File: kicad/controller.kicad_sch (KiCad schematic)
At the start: 33 parts, among them M5 Motor_DC, M6 Motor_DC, M7 Motor_DC, M8 Motor_DC, U10 DRV8833PW, U6 ESP32-DEVKITC, U8 GY-521

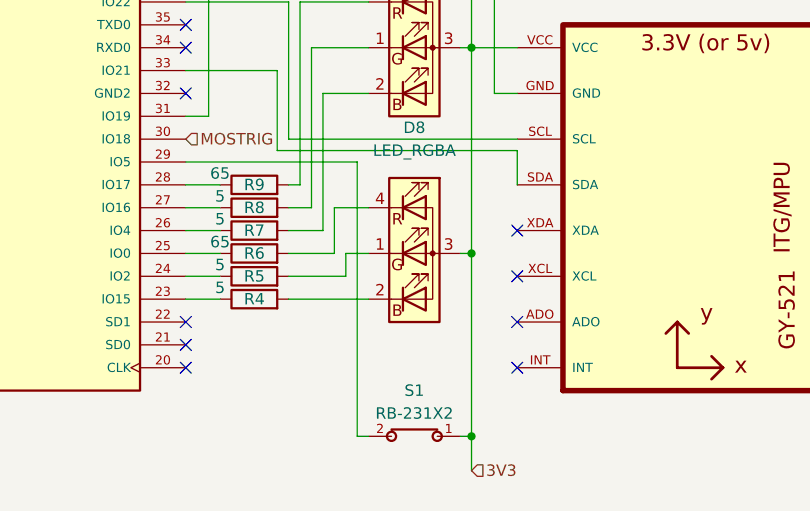
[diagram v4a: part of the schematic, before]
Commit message: Add tilt switch
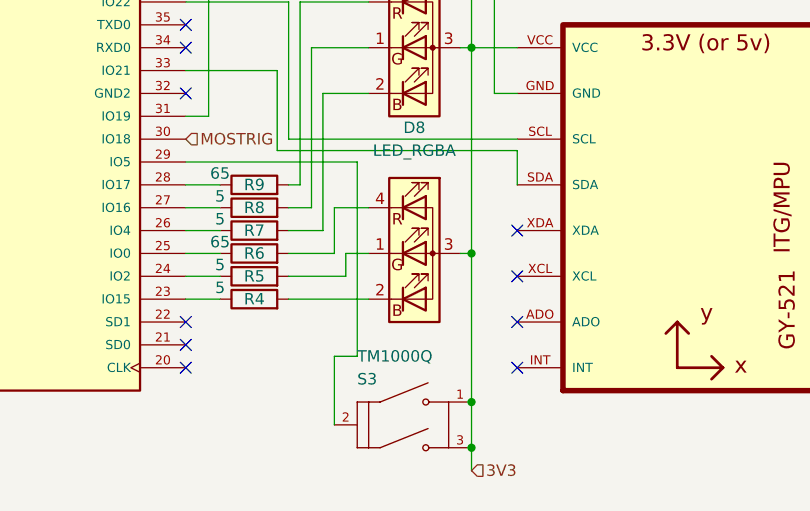
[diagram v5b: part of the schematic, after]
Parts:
- removed S1: RB-231X2, RB-231X2:SW_RB-231X2, symbol RB-231X2:RB-231X2
- added S3: TM1000Q, TM1000Q:SW_TM1000Q, symbol TM1000Q:TM1000Q
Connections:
- net 3V3: now also S3.1, S3.3
- net at U6.29 (IO5): now also S3.2
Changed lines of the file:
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@@
   (junction (at 115.57 74.93) (diameter 0) (color 0 0 0 0)
   )
+  (junction (at 213.36 139.7) (diameter 0) (color 0 0 0 0)
+  )
   (junction (at 125.73 87.63) (diameter 0) (color 0 0 0 0)
   )
@@
   (junction (at 124.46 107.95) (diameter 0) (color 0 0 0 0)
   )
+  (junction (at 213.36 134.62) (diameter 0) (color 0 0 0 0)
+  )
   (junction (at 125.73 127) (diameter 0) (color 0 0 0 0)
   )
@@
   )
   (junction (at 181.61 85.09) (diameter 0) (color 0 0 0 0)
-  )
-  (junction (at 213.36 138.43) (diameter 0) (color 0 0 0 0)
   )
   (junction (at 213.36 95.25) (diameter 0) (color 0 0 0 0)
@@
     (stroke (width 0) (type default))
   )
+  (wire (pts (xy 213.36 139.7) (xy 213.36 142.24))
+    (stroke (width 0) (type default))
+  )
   (wire (pts (xy 77.47 63.5) (xy 77.47 127))
     (stroke (width 0) (type default))
@@
     (stroke (width 0) (type default))
   )
-  (wire (pts (xy 212.09 138.43) (xy 213.36 138.43))
-    (stroke (width 0) (type default))
-  )
   (wire (pts (xy 80.01 74.93) (xy 76.2 74.93))
     (stroke (width 0) (type default))
@@
     (stroke (width 0) (type default))
   )
-  (wire (pts (xy 213.36 118.11) (xy 213.36 138.43))
+  (wire (pts (xy 213.36 118.11) (xy 213.36 134.62))
     (stroke (width 0) (type default))
   )
@@
     (stroke (width 0) (type default))
   )
+  (wire (pts (xy 213.36 134.62) (xy 213.36 139.7))
+    (stroke (width 0) (type default))
+  )
   (wire (pts (xy 121.92 92.71) (xy 121.92 96.52))
     (stroke (width 0) (type default))
@@
     (stroke (width 0) (type default))
   )
-  (wire (pts (xy 213.36 138.43) (xy 213.36 142.24))
-    (stroke (width 0) (type default))
-  )
   (wire (pts (xy 194.31 110.49) (xy 194.31 90.17))
     (stroke (width 0) (type default))
@@
     (stroke (width 0) (type default))
   )
-  (wire (pts (xy 200.66 107.95) (xy 200.66 138.43))
+  (wire (pts (xy 200.66 107.95) (xy 200.66 129.54))
     (stroke (width 0) (type default))
   )
@@
     (stroke (width 0) (type default))
   )
-  (wire (pts (xy 200.66 138.43) (xy 201.93 138.43))
+  (wire (pts (xy 198.12 129.54) (xy 198.12 137.16))
     (stroke (width 0) (type default))
   )
@@
   )
   (wire (pts (xy 57.15 77.47) (xy 80.01 77.47))
+    (stroke (width 0) (type default))
+  )
+  (wire (pts (xy 200.66 129.54) (xy 198.12 129.54))
     (stroke (width 0) (type default))
   )
@@
     )
   )
+  (symbol (lib_id "TM1000Q:TM1000Q") (at 205.74 137.16 0) (unit 1)
+    (in_bom yes) (on_board yes) (dnp no)
+    (property "Reference" "S3" (at 200.66 132.08 0)
+      (effects (font (size 1.27 1.27)) (justify left))
+    )
+    (property "Value" "TM1000Q" (at 200.66 129.54 0)
+      (effects (font (size 1.27 1.27)) (justify left))
+    )
+    (property "Footprint" "TM1000Q:SW_TM1000Q" (at 205.74 137.16 0)
+      (effects (font (size 1.27 1.27)) (justify bottom) hide)
+    )
+    (property "Datasheet" "" (at 205.74 137.16 0)
+      (effects (font (size 1.27 1.27)) hide)
+    )
+    (property "MF" "E-Switch" (at 205.74 137.16 0)
+      (effects (font (size 1.27 1.27)) (justify bottom) hide)
+    )
+    (property "MAXIMUM_PACKAGE_HEIGHT" "6.5mm" (at 205.74 137.16 0)
+      (effects (font (size 1.27 1.27)) (justify bottom) hide)
+    )
+    (property "Package" "SIP-3 E-Switch" (at 205.74 137.16 0)
+      (effects (font (size 1.27 1.27)) (justify bottom) hide)
+    )
+    (property "Price" "None" (at 205.74 137.16 0)
+      (effects (font (size 1.27 1.27)) (justify bottom) hide)
+    )
+    (property "Check_prices" "https://www.snapeda.com/parts/TM1000Q/E-Switch/view-part/?ref=eda" (at 205.74 137.16 0)
+      (effects (font (size 1.27 1.27)) (justify bottom) hide)
+    )
+    (property "STANDARD" "Manufacturer Recommendations" (at 205.74 137.16 0)
+      (effects (font (size 1.27 1.27)) (justify bottom) hide)
+    )
+    (property "PARTREV" "-" (at 205.74 137.16 0)
+      (effects (font (size 1.27 1.27)) (justify bottom) hide)
+    )
+    (property "SnapEDA_Link" "https://www.snapeda.com/parts/TM1000Q/E-Switch/view-part/?ref=snap" (at 205.74 137.16 0)
+      (effects (font (size 1.27 1.27)) (justify bottom) hide)
+    )
+    (property "MP" "TM1000Q" (at 205.74 137.16 0)
+      (effects (font (size 1.27 1.27)) (justify bottom) hide)
+    )
+    (property "Purchase-URL" "https://www.snapeda.com/api/url_track_click_mouser/?unipart_id=649122&manufacturer=E-Switch&part_name=TM1000Q&search_term=tm1000q" (at 205.74 137.16 0)
+      (effects (font (size 1.27 1.27)) (justify bottom) hide)
+    )
+    (property "Description" "\nSWITCH TILT SPST\n" (at 205.74 137.16 0)
+      (effects (font (size 1.27 1.27)) (justify bottom) hide)
+    )
+    (property "MANUFACTURER" "E-Switch" (at 205.74 137.16 0)
+      (effects (font (size 1.27 1.27)) (justify bottom) hide)
+    )
+    (property "Availability" "In Stock" (at 205.74 137.16 0)
+      (effects (font (size 1.27 1.27)) (justify bottom) hide)
+    )
+    (property "SNAPEDA_PN" "TM1000Q" (at 205.74 137.16 0)
+      (effects (font (size 1.27 1.27)) (justify bottom) hide)
+    )
+    (pin "1")
+    (pin "2")
+    (pin "3")
+    (instances
+      (project "robot"
+        (path "/9f6eb88e-d254-4b8d-b64f-838940a89234/50902c9c-c184-4e8b-b7c8-1add935d161c"
+          (reference "S3") (unit 1)
+        )
+        (path "/9f6eb88e-d254-4b8d-b64f-838940a89234/50902c9c-c184-4e8b-b7c8-1add935d161c/8bca0bb0-49b9-4104-9510-11a298d1fb37"
+          (reference "S1") (unit 1)
+        )
+      )
+    )
+  )
   (symbol (lib_id "Motor:Motor_DC") (at 57.15 85.09 0) (unit 1)
     (in_bom yes) (on_board yes) (dnp no) (fields_autoplaced)
@@
         )
       )
-    )
-  )
-  (symbol (lib_id "RB-231X2:RB-231X2") (at 207.01 138.43 0) (unit 1)
-    (in_bom yes) (on_board yes) (dnp no) (fields_autoplaced)
-    (property "Reference" "S1" (at 207.01 133.35 0)
-      (effects (font (size 1.27 1.27)))
-    )
-    (property "Value" "RB-231X2" (at 207.01 135.89 0)
-      (effects (font (size 1.27 1.27)))
-    )
-    (property "Footprint" "RB-231X2:SW_RB-231X2" (at 207.01 138.43 0)
-      (effects (font (size 1.27 1.27)) (justify bottom) hide)
-    )
-    (property "Datasheet" "" (at 207.01 138.43 0)
-      (effects (font (size 1.27 1.27)) hide)
-    )
-    (property "MF" "C&K" (at 207.01 138.43 0)
-      (effects (font (size 1.27 1.27)) (justify bottom) hide)
-    )
-    (property "Description" "\nRolling Ball Tilt Switches\n" (at 207.01 138.43 0)
-      (effects (font (size 1.27 1.27)) (justify bottom) hide)
-    )
-    (property "Package" "Radial Side View  C&amp;K Components" (at 207.01 138.43 0)
-      (effects (font (size 1.27 1.27)) (justify bottom) hide)
-    )
-    (property "Price" "None" (at 207.01 138.43 0)
-      (effects (font (size 1.27 1.27)) (justify bottom) hide)
-    )
-    (property "Check_prices" "https://www.snapeda.com/parts/RB-231X2/C%2526K/view-part/?ref=eda" (at 207.01 138.43 0)
-      (effects (font (size 1.27 1.27)) (justify bottom) hide)
-    )
-    (property "SnapEDA_Link" "https://www.snapeda.com/parts/RB-231X2/C%2526K/view-part/?ref=snap" (at 207.01 138.43 0)
-      (effects (font (size 1.27 1.27)) (justify bottom) hide)
-    )
-    (property "MP" "RB-231X2" (at 207.01 138.43 0)
-      (effects (font (size 1.27 1.27)) (justify bottom) hide)
-    )
-    (property "Purchase-URL" "https://www.snapeda.com/api/url_track_click_mouser/?unipart_id=494671&manufacturer=C&amp;K&part_name=RB-231X2&search_term=rb231" (at 207.01 138.43 0)
-      (effects (font (size 1.27 1.27)) (justify bottom) hide)
-    )
-    (property "Availability" "In Stock" (at 207.01 138.43 0)
-      (effects (font (size 1.27 1.27)) (justify bottom) hide)
-    )
-    (property "MANUFACTURER" "CnK" (at 207.01 138.43 0)
-      (effects (font (size 1.27 1.27)) (justify bottom) hide)
-    )
-    (pin "1")
-    (pin "2")
-    (instances
-      (project "robot"
-        (path "/9f6eb88e-d254-4b8d-b64f-838940a89234/50902c9c-c184-4e8b-b7c8-1add935d161c"
-          (reference "S1") (unit 1)
-        )
-        (path "/9f6eb88e-d254-4b8d-b64f-838940a89234/50902c9c-c184-4e8b-b7c8-1add935d161c/8bca0bb0-49b9-4104-9510-11a298d1fb37"
-          (reference "S2") (unit 1)
-        )
-      )

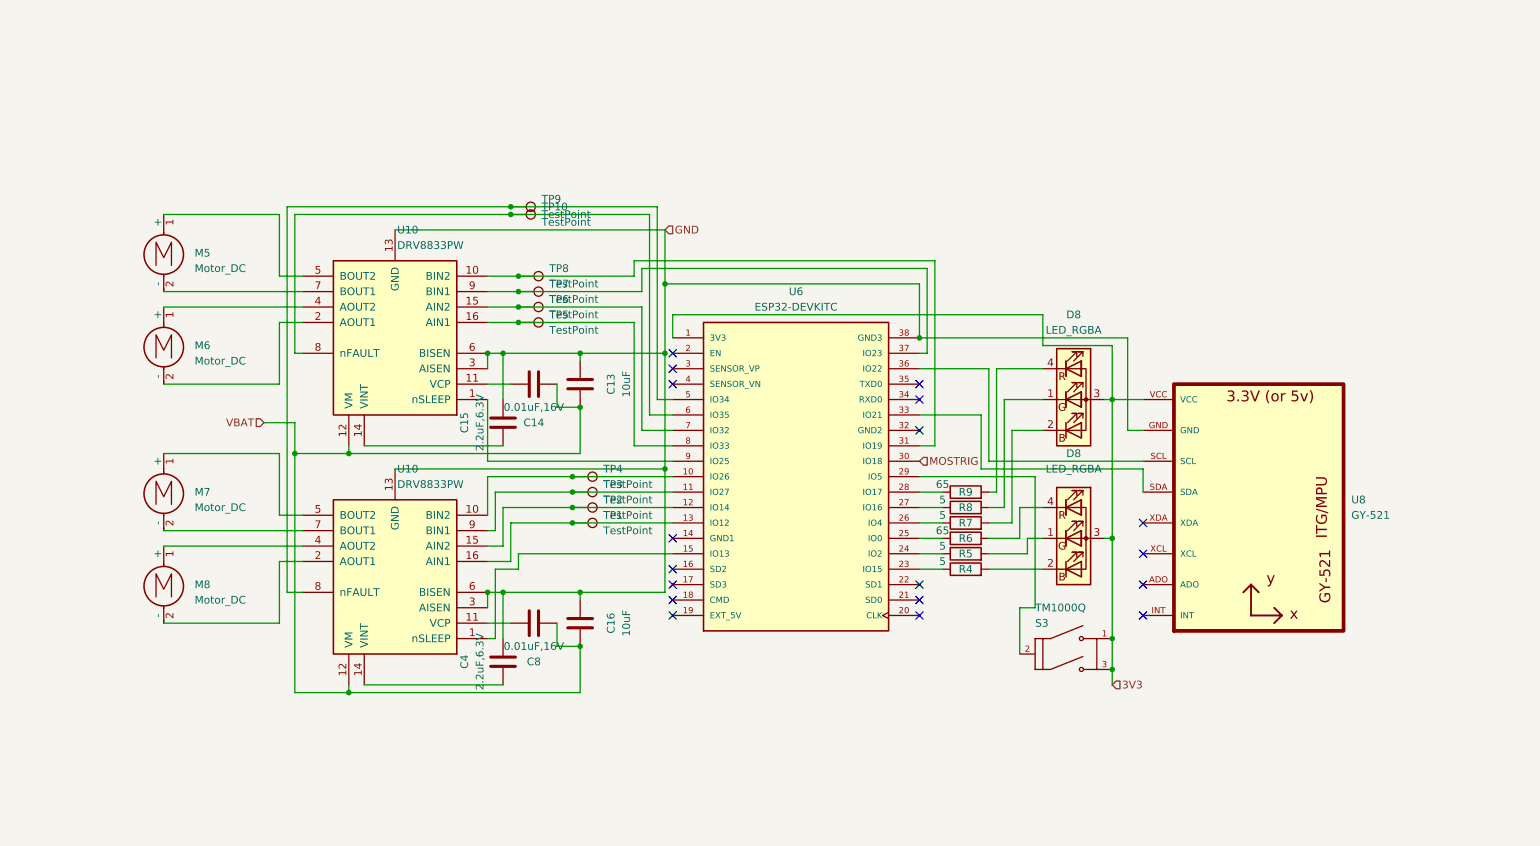
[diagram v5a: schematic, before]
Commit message: Fix banned pins on ESP32
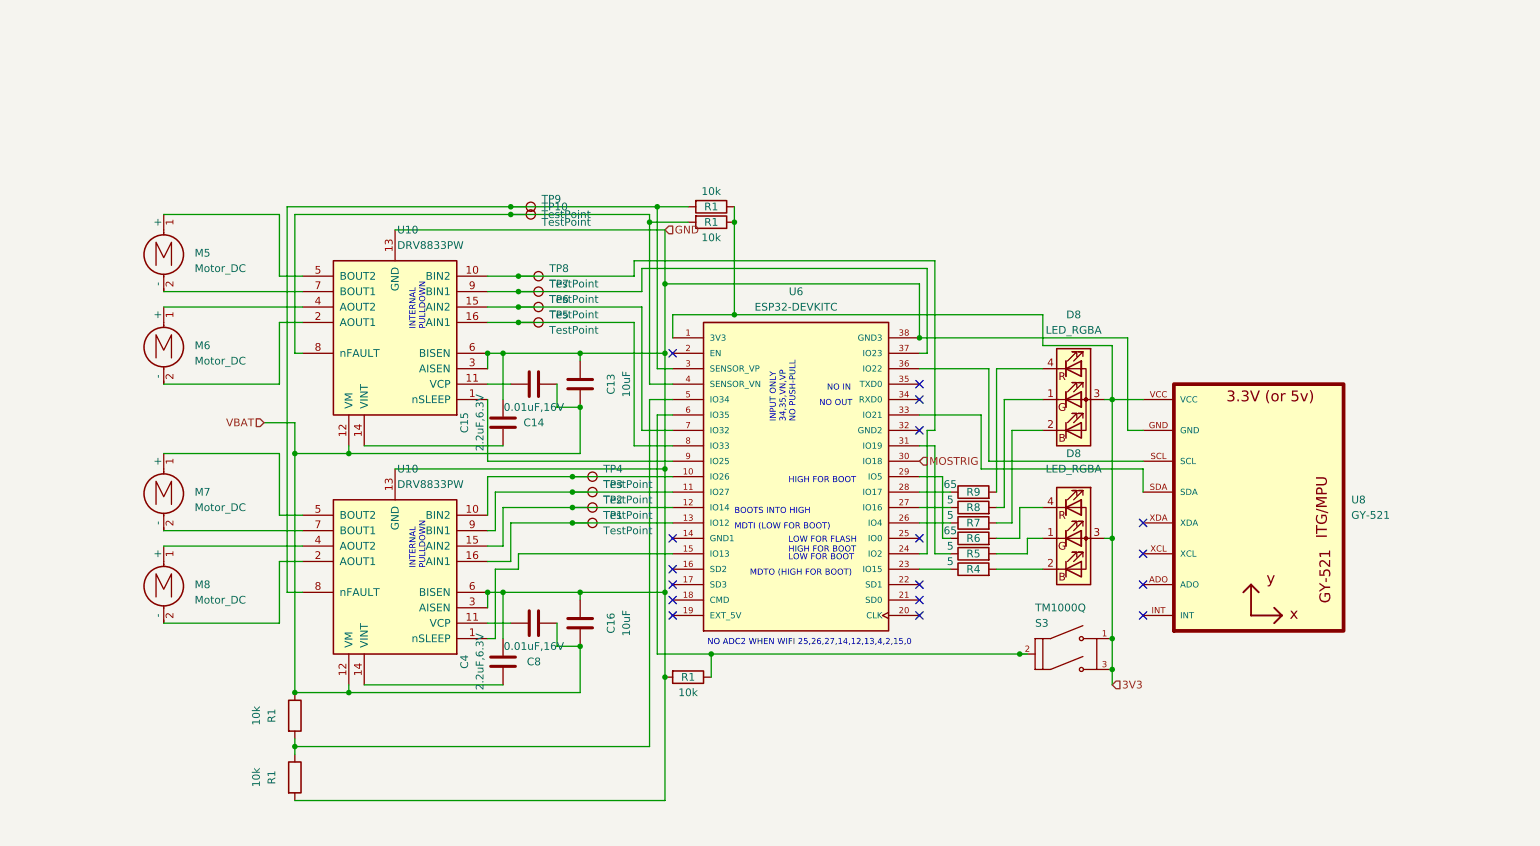
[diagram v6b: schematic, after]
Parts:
- added R1 (x5): 10k, Resistor_SMD:R_0805_2012Metric_Pad1.20x1.40mm_HandSolder, symbol Device:R
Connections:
- net 3V3: now also R1.1, R1.1
- net GND: now also R1.2, R1.2
- net VBAT: now also R1.1
- net at TP10.1, U10.8 (nFAULT): now also U6.4 (SENSOR_VN), R1.2; no longer U6.6 (IO35)
- net at TP8.1, U10.10 (BIN2): now also U6.24 (IO2); no longer U6.31 (IO19)
- net at R6.1: now also U6.29 (IO5); no longer U6.25 (IO0)
- net at R5.1: now also U6.31 (IO19); no longer U6.24 (IO2)
- net at S3.2: now also U6.6 (IO35), R1.1; no longer U6.29 (IO5)
- net at U6.3 (SENSOR_VP): now also TP9.1, U10.8 (nFAULT), R1.2
- new net: R1.1, R1.2, U6.5 (IO34)
- no-connect marks 18 -> 17
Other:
- note added: "BOOTS INTO HIGH"
- note added: "HIGH FOR BOOT"
- note added: "INPUT ONLY 34,35,VN,VP NO PUSH-PULL"
- note added: "INTERNAL PULLDOWN"
- note added: "LOW FOR BOOT"
- note added: "LOW FOR FLASH HIGH FOR BOOT"
- note added: "MDTI (LOW FOR BOOT)"
- note added: "MDTO (HIGH FOR BOOT)"
- note added: "NO ADC2 WHEN WIFI 25,26,27,14,12,13,4,2,15,0"
- note added: "NO IN"
- note added: "NO OUT"
- moved on the sheet: R4, R5, R6, R7, R8, R9

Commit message: Make schematic pretty
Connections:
- net SCL: now reaches U6.36 (IO22), U8.SCL
- net SDA: now reaches U6.33 (IO21), U8.SDA
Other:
- note added: "IMU"
- note added: "MOTOR DRIVER"
- note added: "POWER MONITORING"
- note added: "RGB LEDS R - 2.0V G - 3.2V B - 3.2V"
- moved on the sheet: C13, C14, C15, C16, C4, C8, D8, M5, M6, M7, M8, R1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

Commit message: Final PCB
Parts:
- D8: value LED_RGBA -> QBL8RGB60D0-2897
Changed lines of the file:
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@@
       (effects (font (size 1.27 1.27)))
     )
-    (property "Value" "LED_RGBA" (at 260.35 83.82 0)
-      (effects (font (size 1.27 1.27)))
+    (property "Value" "QBL8RGB60D0-2897" (at 260.35 83.82 0)
+      (effects (font (size 1.27 1.27)) hide)
     )
     (property "Footprint" "Connector_PinSocket_2.54mm:PinSocket_1x04_P2.54mm_Vertical" (at 260.35 96.52 0)
@@
       (effects (font (size 1.27 1.27)))
     )
-    (property "Value" "LED_RGBA" (at 260.35 106.68 0)
-      (effects (font (size 1.27 1.27)))
+    (property "Value" "QBL8RGB60D0-2897\n" (at 260.35 106.68 0)
+      (effects (font (size 1.27 1.27)) hide)
     )
     (property "Footprint" "Connector_PinSocket_2.54mm:PinSocket_1x04_P2.54mm_Vertical" (at 260.35 119.38 0)
